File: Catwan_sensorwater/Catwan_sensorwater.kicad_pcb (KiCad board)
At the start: 2 copper layers, 65 x 50 mm, 40 parts, among them J1 SENSOR 1, J10 VSP, J2 SENSOR 2, J3 SENSOR 3, J4 BATT, J5 USB_B, J6 Conn_01x04, J7 Conn_01x03, J8 Conn_01x03_Female, J9 SENSOR 4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

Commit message: Microcontroller GND
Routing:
- net GND: track 164.9 -> 217.7 mm, vias 11 -> 19
- net /DIO0: track 0.49 -> 32.5 mm, vias 0 -> 2
- net Net-(J2-Pad2): track 11.7 -> 27.1 mm, vias 0 -> 2
- net Net-(J3-Pad2): track 12.8 -> 23.5 mm, vias 0 -> 2
- net Net-(J9-Pad2): track 33.9 -> 31.2 mm
- net /SENS_Y: track 17.2 -> 19.3 mm
- net /DIO2: track 26.1 -> 24.0 mm
- net /MOSI: track 12.6 -> 12.3 mm, vias 0 -> 2

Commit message: Changes GND
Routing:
- net GND: track 217.7 -> 235.3 mm, vias 19 -> 16
- net +3V3: track 123.0 -> 120.6 mm, vias 6 -> 3

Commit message: Check rooteo
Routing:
- net GND: track 235.3 -> 261.8 mm, vias 16 -> 13
- net Net-(J9-Pad2): track 31.2 -> 32.3 mm
- net Net-(J3-Pad2): track 23.5 -> 24.5 mm
- net Net-(J9-Pad1): track 27.7 -> 28.4 mm
- net /SENS_X: track 8.22 -> 8.72 mm

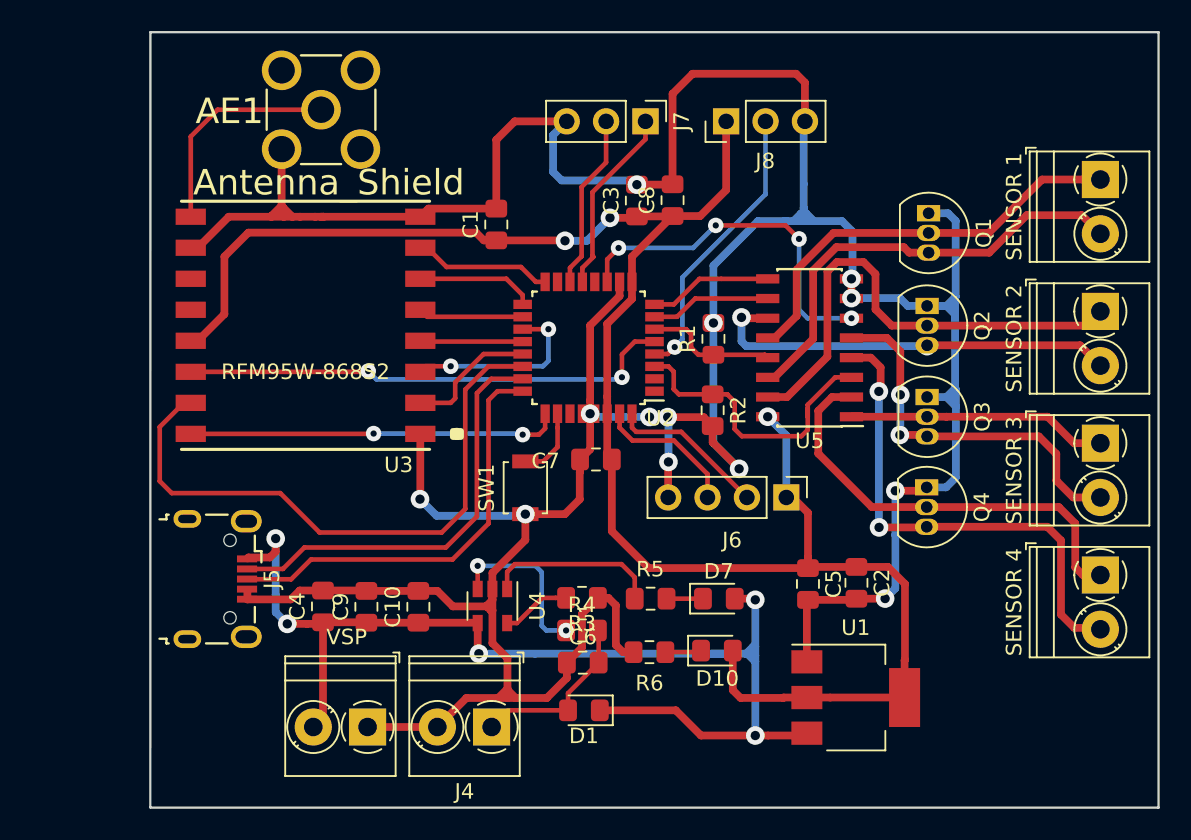
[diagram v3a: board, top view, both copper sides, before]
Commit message: Track correction
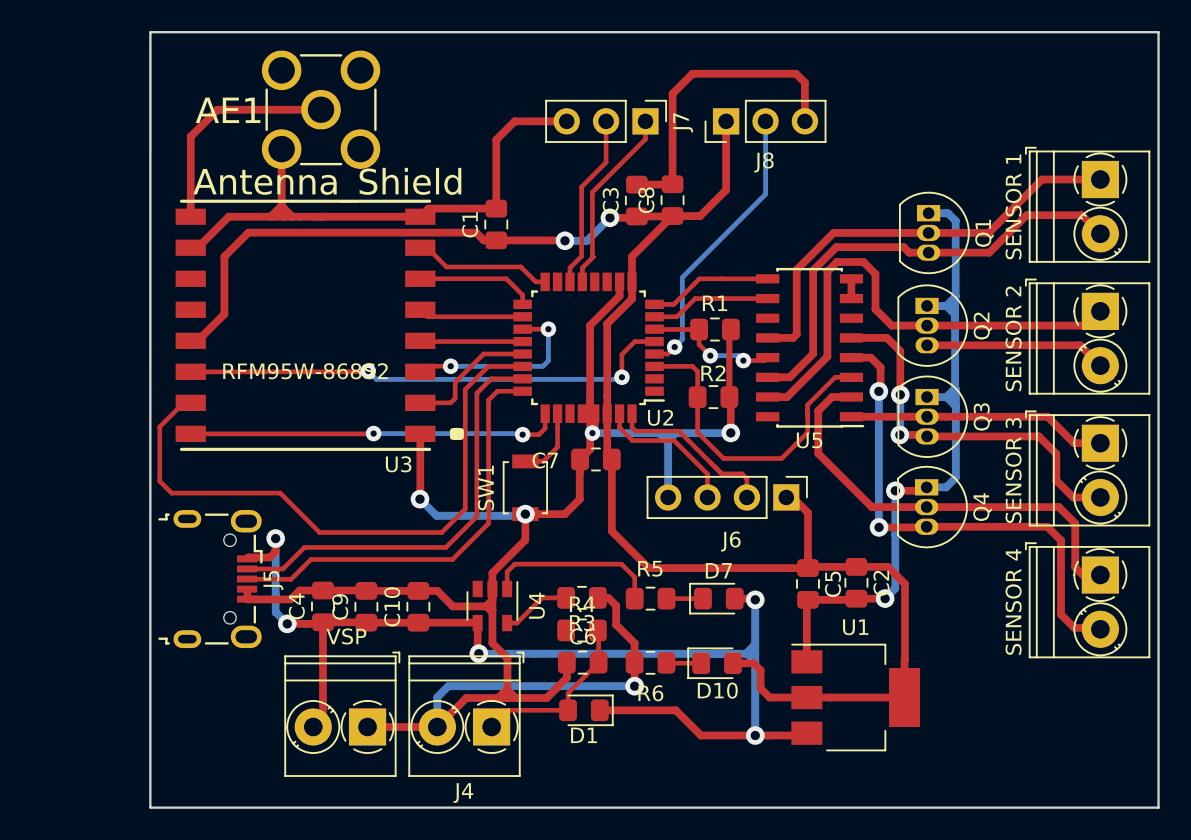
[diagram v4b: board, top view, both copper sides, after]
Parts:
- moved R2 0.85 mm to (151.3, 103.5), turned to 0 degrees
- moved D10 0.82 mm to (151.5, 120.7)
- moved R6 0.69 mm to (147.2, 120.7)
- moved R1 0.61 mm to (151.4, 99.2), turned to 0 degrees
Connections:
- AE1 pad 4: (no net) -> GND
- AE1 pad 5: (no net) -> GND
- AE1 pad E: (no net) -> GND
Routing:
- net GND: track 261.8 -> 228.7 mm, vias 13 -> 7
- net /EN: track 23.3 -> 0.00 mm, vias 4 -> 0
- net Net-(J2-Pad2): track 27.1 -> 11.7 mm, vias 2 -> 0
- net Net-(R4-Pad1): track 10.9 -> 0.00 mm, vias 2 -> 0
- net +3V3: track 120.9 -> 114.0 mm, vias 3 -> 2
- net /SENS_Y: track 19.3 -> 21.2 mm
- net /SWDIO: track 10.2 -> 11.7 mm
- net Net-(J1-Pad2): track 29.2 -> 30.2 mm
- net Net-(J1-Pad1): track 27.4 -> 28.1 mm
- net /SENS_X: track 8.72 -> 8.94 mm, vias 0 -> 2

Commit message: Adapter capacitor and diode
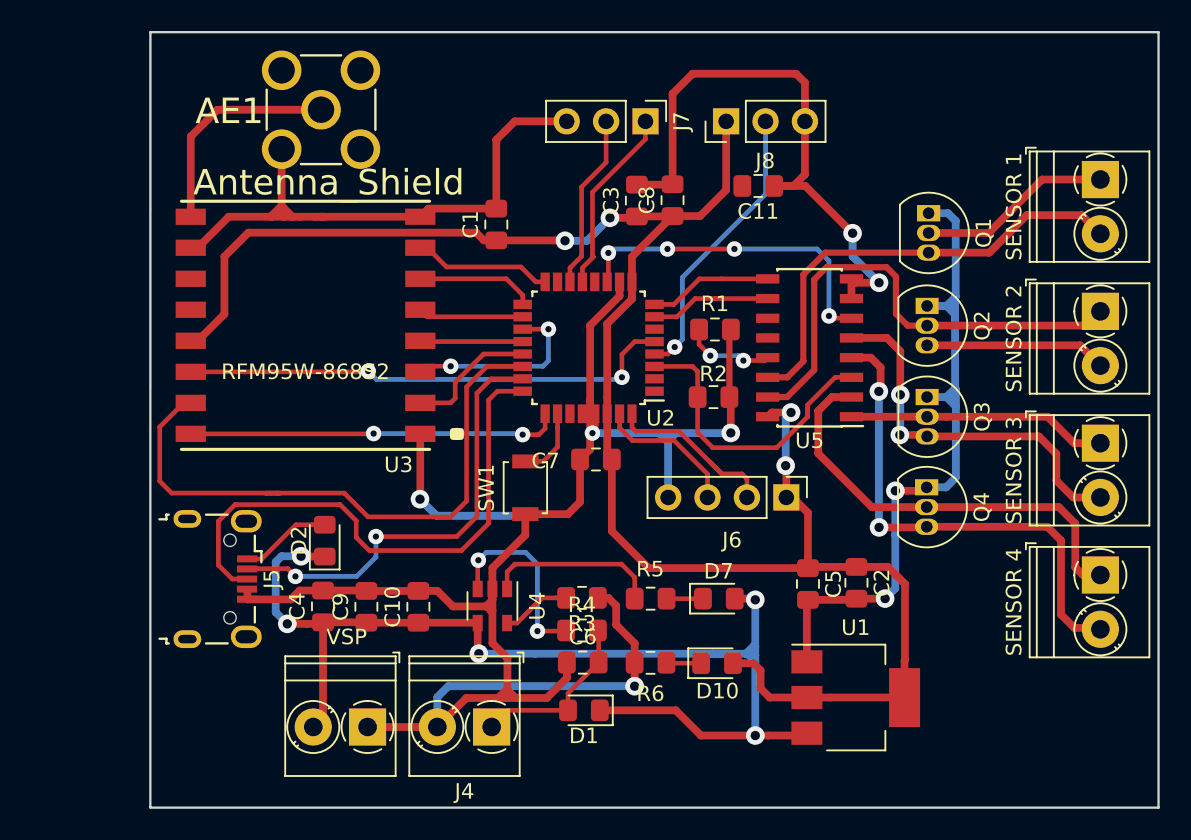
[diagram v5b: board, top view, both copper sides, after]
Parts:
- added C11: 1uF, Capacitor_SMD:C_0805_2012Metric_Pad1.15x1.40mm_HandSolder, F.Cu at (154.2, 89.9)
- added D2: D_Schottky, Diode_SMD:D_0805_2012Metric_Pad1.15x1.40mm_HandSolder, F.Cu at (126.2, 112.8)
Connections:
- AE1 pad 4: GND -> (no net)
- AE1 pad 5: GND -> (no net)
- AE1 pad E: GND -> (no net)
- J5 pad 1: VCC -> Net-(D2-Pad2)
- U2 pad 29: GND -> Net-(C11-Pad2)
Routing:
- net /EN: track 0.00 -> 21.6 mm, vias 0 -> 4
- net GND: track 228.7 -> 246.5 mm, vias 7 -> 8
- net Net-(J1-Pad1): track 28.1 -> 12.5 mm
- net Net-(R4-Pad1): track 0.00 -> 12.4 mm, vias 0 -> 2
- net /D+: track 27.4 -> 35.9 mm
- net +3V3: track 114.0 -> 121.2 mm, vias 2 -> 4
- net Net-(D2-Pad2): track 0.00 -> 5.92 mm
- net /SENS_X: track 8.94 -> 6.08 mm
- net /D-: track 27.5 -> 28.7 mm, vias 0 -> 2
- net /SENS_Y: track 21.2 -> 20.0 mm
- net VCC: track 75.0 -> 73.9 mm

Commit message: Routeo changes with new footprint
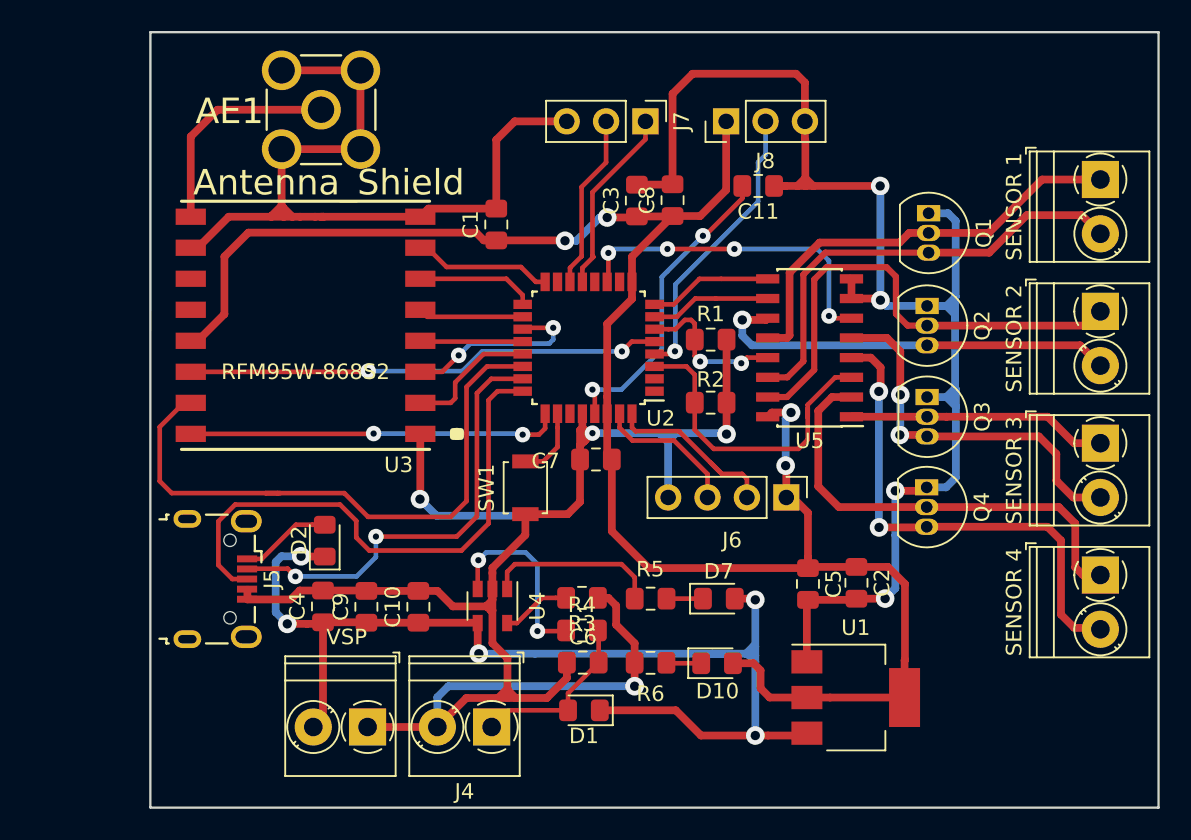
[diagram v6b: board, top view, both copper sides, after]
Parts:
- moved R1 0.71 mm to (151.1, 99.8)
- moved R2 0.40 mm to (151.1, 103.9)
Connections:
- AE1 pad 4: (no net) -> GND
- AE1 pad 5: (no net) -> GND
- AE1 pad E: (no net) -> GND
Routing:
- net Net-(C11-Pad2): track 0.00 -> 19.9 mm, vias 0 -> 2
- net Net-(J1-Pad1): track 12.5 -> 28.1 mm
- net Net-(J2-Pad2): track 11.7 -> 26.6 mm, vias 0 -> 1
- net GND: track 246.5 -> 259.5 mm
- net /SENS_X: track 6.08 -> 10.3 mm
- net /DIO0: track 32.5 -> 31.2 mm
- net Net-(J9-Pad1): track 28.4 -> 29.6 mm
- net /SENS_Y: track 20.0 -> 20.8 mm

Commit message: Netlist D3
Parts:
- added D3: D_Schottky, Diode_SMD:D_0805_2012Metric_Pad1.15x1.40mm_HandSolder, F.Cu at (109.2, 87.6)
- C10: value 100nf -> 10uF
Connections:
- AE1 pad 4: GND -> (no net)
- AE1 pad 5: GND -> (no net)
- AE1 pad E: GND -> (no net)
- J10 pad 2: VCC -> /Vsp
- U4 pad 3: Net-(R4-Pad1) -> /BAT
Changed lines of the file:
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@@
     (tracks 587)
     (zones 0)
-    (modules 42)
-    (nets 50)
+    (modules 43)
+    (nets 51)
   )
   (page A4)
@@
   (net 48 "Net-(C11-Pad2)")
   (net 49 "Net-(D2-Pad2)")
+  (net 50 /Vsp)
   (net_class Default "This is the default net class."
     (clearance 0.2)
@@
     (add_net /SWDIO)
     (add_net /Tx)
+    (add_net /Vsp)
     (add_net "Net-(AE1-Pad1)")
     (add_net "Net-(C11-Pad2)")
@@
       (net 2 GND) (solder_mask_margin 0.2))
     (pad E thru_hole circle (at -2.54 2.54 90) (size 2.5527 2.5527) (drill 1.7018) (layers *.Cu *.Mask F.SilkS)
-      (net 2 GND) (solder_mask_margin 0.2))
+      (solder_mask_margin 0.2))
     (pad 4 thru_hole circle (at 2.54 2.54 90) (size 2.5527 2.5527) (drill 1.7018) (layers *.Cu *.Mask F.SilkS)
-      (net 2 GND) (solder_mask_margin 0.2))
+      (solder_mask_margin 0.2))
     (pad 5 thru_hole circle (at 2.54 -2.54 90) (size 2.5527 2.5527) (drill 1.7018) (layers *.Cu *.Mask F.SilkS)
-      (net 2 GND) (solder_mask_margin 0.2))
+      (solder_mask_margin 0.2))
   )
   (module Capacitor_SMD:C_0805_2012Metric_Pad1.15x1.40mm_HandSolder (layer F.Cu)
@@
       (effects (font (size 1 1) (thickness 0.15)))
     )
-    (fp_text value 100nf (at 0 1.65 90) (layer F.Fab)
+    (fp_text value 10uF (at 0 1.65 90) (layer F.Fab)
       (effects (font (size 1 1) (thickness 0.15)))
     )
@@
     (fp_arc (start 0 0) (end 0 1.68) (angle -32) (layer F.SilkS) (width 0.12))
     (pad 2 thru_hole circle (at 3.5 0 180) (size 2.4 2.4) (drill 1.2) (layers *.Cu *.Mask)
-      (net 4 VCC))
+      (net 50 /Vsp))
     (pad 1 thru_hole rect (at 0 0 180) (size 2.4 2.4) (drill 1.2) (layers *.Cu *.Mask)
       (net 2 GND))
@@
       (net 2 GND))
     (pad 3 smd rect (at -1.1 0.95 270) (size 1.06 0.65) (layers F.Cu F.Paste F.Mask)
-      (net 24 "Net-(R4-Pad1)"))
+      (net 47 /BAT))
     (pad 4 smd rect (at 1.1 0.95 270) (size 1.06 0.65) (layers F.Cu F.Paste F.Mask)
       (net 4 VCC))
@@
     (model ${KISYS3DMOD}/Diode_SMD.3dshapes/D_0805_2012Metric.wrl
       (at (xyz 0 0 0))
+      (scale (xyz 1 1 1))
+      (rotate (xyz 0 0 0))
+    )
+  )
+  (module Diode_SMD:D_0805_2012Metric_Pad1.15x1.40mm_HandSolder (layer F.Cu)
+    (at 109.22 87.63)
+    (descr "Diode SMD 0805 (2012 Metric), square (rectangular) end terminal, IPC_7351 nominal, (Body size source: https://docs.google.com/spreadsheets/d/1BsfQQcO9C6DZCsRaXUlFlo91Tg2WpOkGARC1WS5S8t0/edit?usp=sharing), generated with kicad-footprint-generator")
+    (tags "diode handsolder")
+    (attr smd)
+    (fp_text reference D3 (at 0 -1.65) (layer F.SilkS)
+      (effects (font (size 1 1) (thickness 0.15)))
+    )
+    (fp_text value D_Schottky (at 0 1.65) (layer F.Fab)
+      (effects (font (size 1 1) (thickness 0.15)))
+    )
+    (fp_line (start 1 -0.6) (end -0.7 -0.6) (layer F.Fab) (width 0.1))
+    (fp_line (start -0.7 -0.6) (end -1 -0.3) (layer F.Fab) (width 0.1))
+    (fp_line (start -1 -0.3) (end -1 0.6) (layer F.Fab) (width 0.1))
+    (fp_line (start -1 0.6) (end 1 0.6) (layer F.Fab) (width 0.1))
+    (fp_line (start 1 0.6) (end 1 -0.6) (layer F.Fab) (width 0.1))
+    (fp_line (start 1 -0.96) (end -1.86 -0.96) (layer F.SilkS) (width 0.12))
+    (fp_line (start -1.86 -0.96) (end -1.86 0.96) (layer F.SilkS) (width 0.12))
+    (fp_line (start -1.86 0.96) (end 1 0.96) (layer F.SilkS) (width 0.12))
+    (fp_line (start -1.85 0.95) (end -1.85 -0.95) (layer F.CrtYd) (width 0.05))
+    (fp_line (start -1.85 -0.95) (end 1.85 -0.95) (layer F.CrtYd) (width 0.05))
+    (fp_line (start 1.85 -0.95) (end 1.85 0.95) (layer F.CrtYd) (width 0.05))
+    (fp_line (start 1.85 0.95) (end -1.85 0.95) (layer F.CrtYd) (width 0.05))
+    (fp_text user %R (at 0 0) (layer F.Fab)
+      (effects (font (size 0.5 0.5) (thickness 0.08)))
+    )
+    (pad 1 smd roundrect (at -1.025 0) (size 1.15 1.4) (layers F.Cu F.Paste F.Mask) (roundrect_rratio 0.217391)
+      (net 4 VCC))
+    (pad 2 smd roundrect (at 1.025 0) (size 1.15 1.4) (layers F.Cu F.Paste F.Mask) (roundrect_rratio 0.217391)
+      (net 50 /Vsp))
+    (model ${KISYS3DMOD}/Diode_SMD.3dshapes/D_0805_2012Metric.wrl
+      (at (xyz 0 0 0))

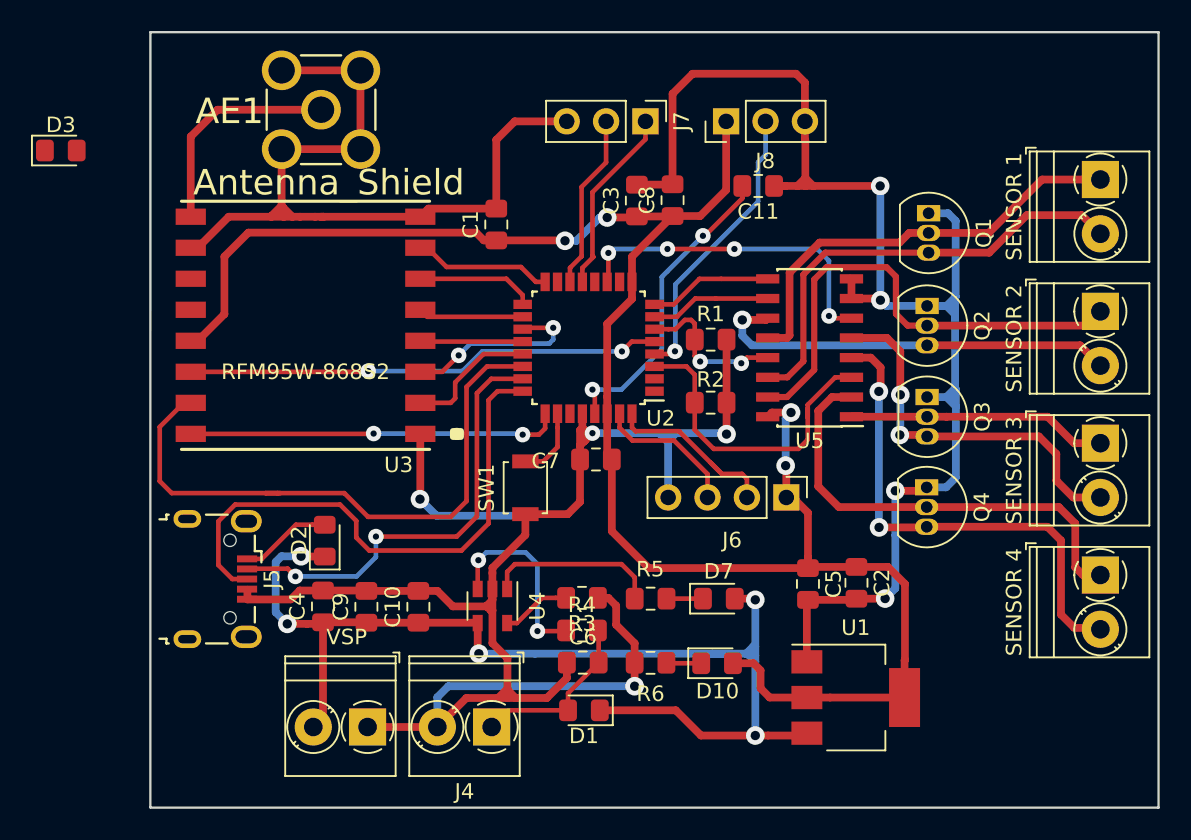
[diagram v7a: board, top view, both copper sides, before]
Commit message: Add D3 PCB
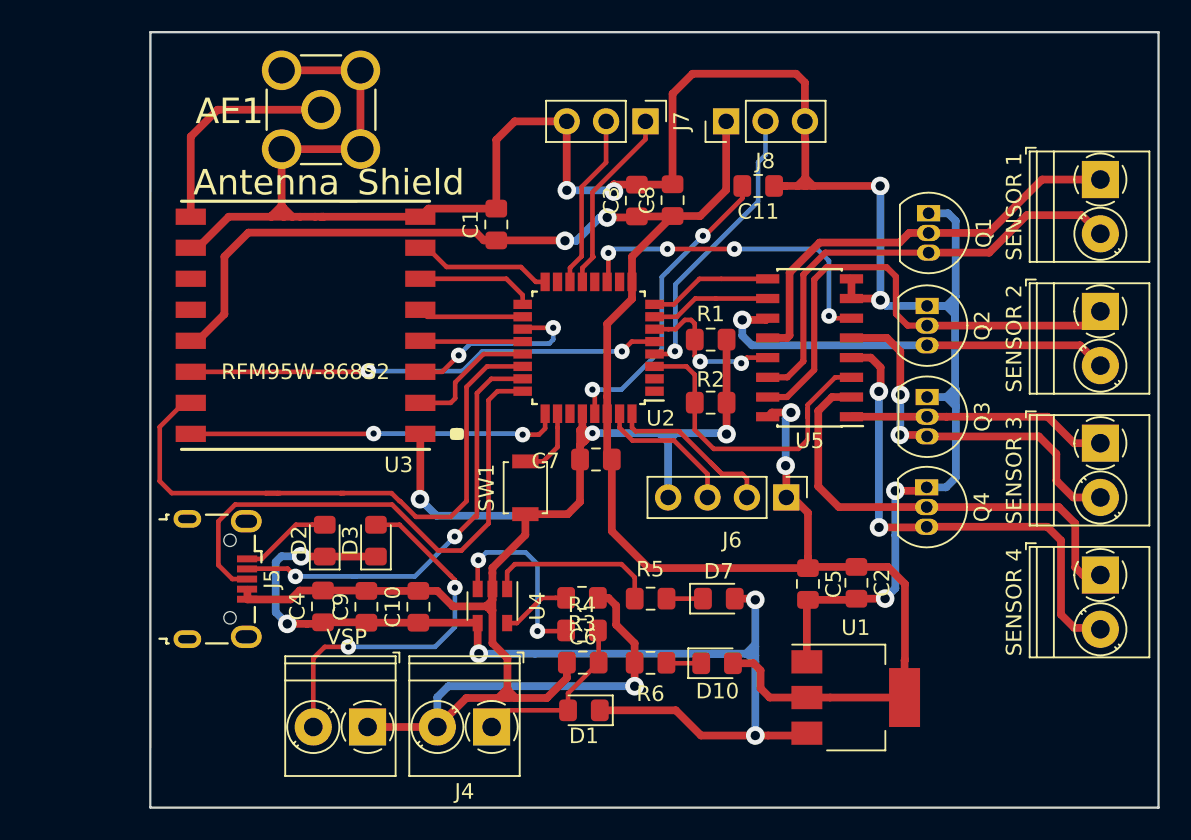
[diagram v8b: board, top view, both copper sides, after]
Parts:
- moved D3 32.3 mm to (129.5, 112.8), turned to 90 degrees
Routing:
- net /Vsp: track 0.00 -> 24.9 mm, vias 0 -> 2
- net GND: track 259.5 -> 269.0 mm, vias 8 -> 10
- net VCC: track 73.9 -> 70.2 mm
- net /D+: track 35.9 -> 35.2 mm
